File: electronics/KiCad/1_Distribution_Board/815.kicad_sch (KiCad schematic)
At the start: 10 parts, among them J1 Conn_02x08_Odd_Even, J40 Module Right, J42 Signals 0-3, J43 Signals 4-7, J44 Signals 8-11, J45 Conn_01x10, J46 Conn_01x06, J47 Signals 12-15, J48 Module Left

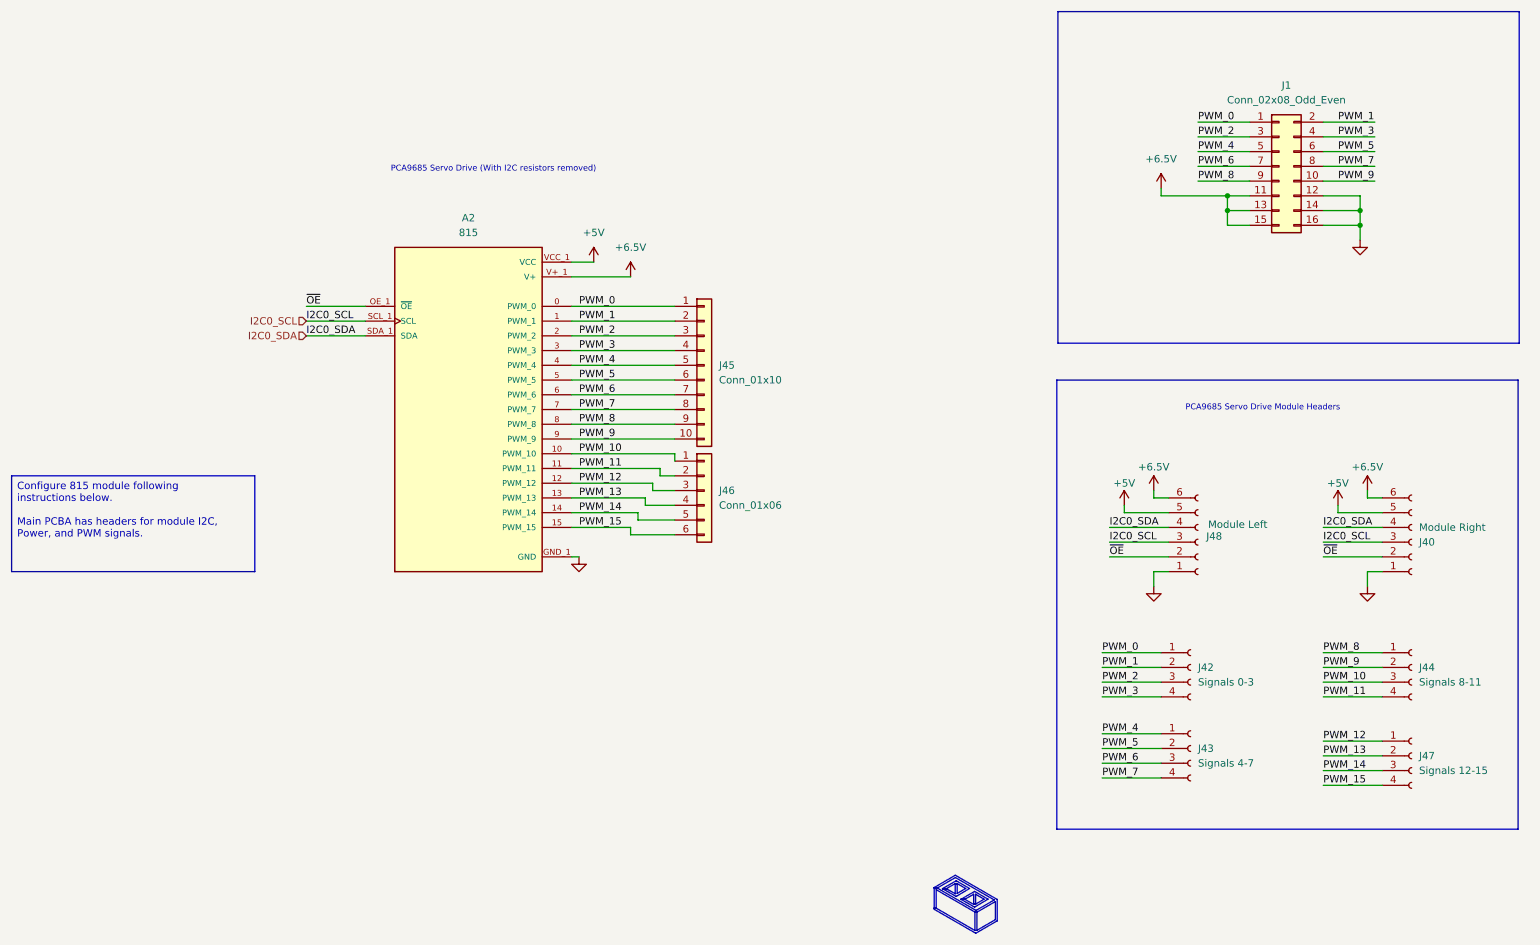
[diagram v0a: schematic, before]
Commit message: PCB updates
Added stepper module headers and working on silk for ease of debug.
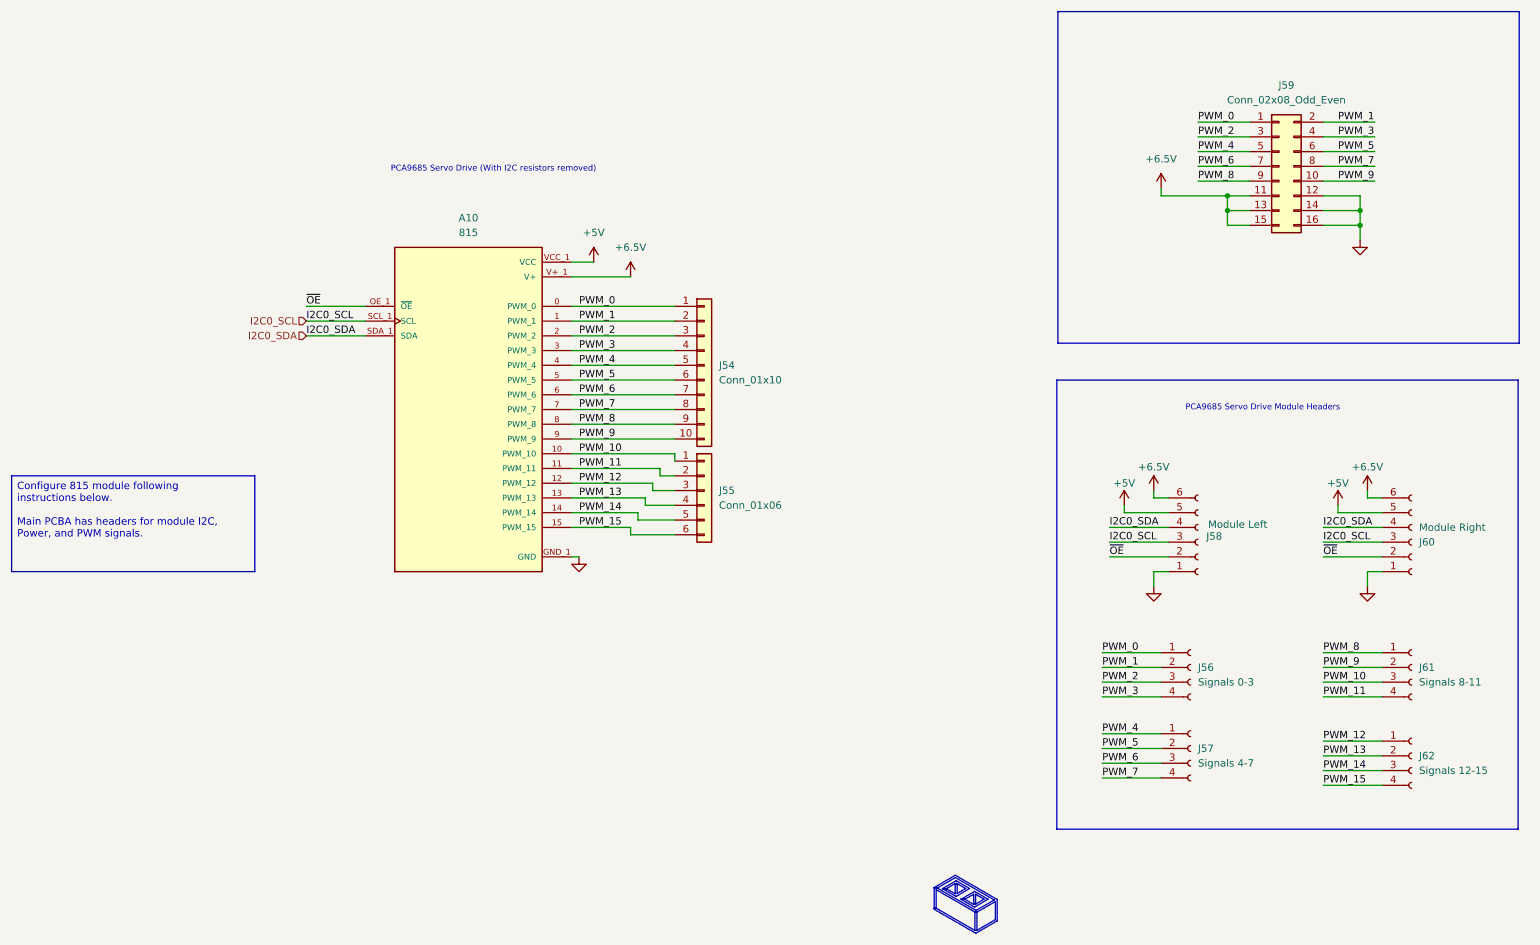
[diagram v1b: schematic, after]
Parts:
- renumbered A2 to A10, J45 to J54, J46 to J55, J42 to J56, J43 to J57, J48 to J58, J1 to J59, J40 to J60, J44 to J61, J47 to J62
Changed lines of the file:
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@@
 		(dnp no)
 		(fields_autoplaced yes)
-		(property "Reference" "J46"
+		(property "Reference" "J55"
 			(at 140.97 101.5999 0)
 			(effects
@@
 			(project "1_Distribution_Board"
 				(path "/d53c8c01-e754-4310-8a73-7d7c95e64cd3/4f60e607-b8a0-4b26-ada7-74dd2d095020"
-					(reference "J46")
+					(reference "J55")
 					(unit 1)
 				)
@@
 		(dnp no)
 		(fields_autoplaced yes)
-		(property "Reference" "#PWR0110"
+		(property "Reference" "#PWR0135"
 			(at 251.46 64.77 0)
 			(effects
@@
 			(project "1_Distribution_Board"
 				(path "/d53c8c01-e754-4310-8a73-7d7c95e64cd3/4f60e607-b8a0-4b26-ada7-74dd2d095020"
-					(reference "#PWR0110")
+					(reference "#PWR0135")
 					(unit 1)
 				)
@@
 		(dnp no)
 		(fields_autoplaced yes)
-		(property "Reference" "#PWR0109"
+		(property "Reference" "#PWR0133"
 			(at 217.17 53.34 0)
 			(effects
@@
 			(project "1_Distribution_Board"
 				(path "/d53c8c01-e754-4310-8a73-7d7c95e64cd3/4f60e607-b8a0-4b26-ada7-74dd2d095020"
-					(reference "#PWR0109")
+					(reference "#PWR0133")
 					(unit 1)
 				)
@@
 		(dnp no)
 		(fields_autoplaced yes)
-		(property "Reference" "J45"
+		(property "Reference" "J54"
 			(at 140.97 80.0099 0)
 			(effects
@@
 			(project "1_Distribution_Board"
 				(path "/d53c8c01-e754-4310-8a73-7d7c95e64cd3/4f60e607-b8a0-4b26-ada7-74dd2d095020"
-					(reference "J45")
+					(reference "J54")
 					(unit 1)
 				)
@@
 		(dnp no)
 		(fields_autoplaced yes)
-		(property "Reference" "J1"
+		(property "Reference" "J59"
 			(at 238.76 31.75 0)
 			(effects
@@
 			(project "1_Distribution_Board"
 				(path "/d53c8c01-e754-4310-8a73-7d7c95e64cd3/4f60e607-b8a0-4b26-ada7-74dd2d095020"
-					(reference "J1")
+					(reference "J59")
 					(unit 1)
 				)
@@
 		(on_board yes)
 		(dnp no)
-		(property "Reference" "#PWR0112"
+		(property "Reference" "#PWR0134"
 			(at 247.65 107.95 0)
 			(effects
@@
 			(project "1_Distribution_Board"
 				(path "/d53c8c01-e754-4310-8a73-7d7c95e64cd3/4f60e607-b8a0-4b26-ada7-74dd2d095020"
-					(reference "#PWR0112")
+					(reference "#PWR0134")
 					(unit 1)
 				)
@@
 		(dnp no)
 		(fields_autoplaced yes)
-		(property "Reference" "J44"
+		(property "Reference" "J61"
 			(at 261.62 132.0799 0)
 			(effects
@@
 			(project "1_Distribution_Board"
 				(path "/d53c8c01-e754-4310-8a73-7d7c95e64cd3/4f60e607-b8a0-4b26-ada7-74dd2d095020"
-					(reference "J44")
+					(reference "J61")
 					(unit 1)
 				)
@@
 		(on_board yes)
 		(dnp no)
-		(property "Reference" "#PWR0113"
+		(property "Reference" "#PWR0136"
 			(at 252.73 105.41 0)
 			(effects
@@
 			(project "1_Distribution_Board"
 				(path "/d53c8c01-e754-4310-8a73-7d7c95e64cd3/4f60e607-b8a0-4b26-ada7-74dd2d095020"
-					(reference "#PWR0113")
+					(reference "#PWR0136")
 					(unit 1)
 				)
@@
 		(dnp no)
 		(fields_autoplaced yes)
-		(property "Reference" "J43"
+		(property "Reference" "J57"
 			(at 223.52 146.0499 0)
 			(effects
@@
 			(project "1_Distribution_Board"
 				(path "/d53c8c01-e754-4310-8a73-7d7c95e64cd3/4f60e607-b8a0-4b26-ada7-74dd2d095020"
-					(reference "J43")
+					(reference "J57")
 					(unit 1)
 				)
@@
 		(dnp no)
 		(fields_autoplaced yes)
-		(property "Reference" "#PWR0111"
+		(property "Reference" "#PWR0137"
 			(at 252.73 124.46 0)
 			(effects
@@
 			(project "1_Distribution_Board"
 				(path "/d53c8c01-e754-4310-8a73-7d7c95e64cd3/4f60e607-b8a0-4b26-ada7-74dd2d095020"
-					(reference "#PWR0111")
+					(reference "#PWR0137")
 					(unit 1)
 				)
@@
 		(dnp no)
 		(fields_autoplaced yes)
-		(property "Reference" "J42"
+		(property "Reference" "J56"
 			(at 223.52 132.0799 0)
 			(effects
@@
 			(project "1_Distribution_Board"
 				(path "/d53c8c01-e754-4310-8a73-7d7c95e64cd3/4f60e607-b8a0-4b26-ada7-74dd2d095020"
-					(reference "J42")
+					(reference "J56")
 					(unit 1)
 				)
@@
 		(dnp no)
 		(fields_autoplaced yes)
-		(property "Reference" "J47"
+		(property "Reference" "J62"
 			(at 261.62 147.3199 0)
 			(effects
@@
 			(project "1_Distribution_Board"
 				(path "/d53c8c01-e754-4310-8a73-7d7c95e64cd3/4f60e607-b8a0-4b26-ada7-74dd2d095020"
-					(reference "J47")
+					(reference "J62")
 					(unit 1)
 				)
@@
 		(dnp no)
 		(fields_autoplaced yes)
-		(property "Reference" "#PWR0116"
+		(property "Reference" "#PWR0132"
 			(at 215.9 124.46 0)
 			(effects
@@
 			(project "1_Distribution_Board"
 				(path "/d53c8c01-e754-4310-8a73-7d7c95e64cd3/4f60e607-b8a0-4b26-ada7-74dd2d095020"
-					(reference "#PWR0116")
+					(reference "#PWR0132")
 					(unit 1)
 				)
@@
 		(dnp no)
 		(fields_autoplaced yes)
-		(property "Reference" "#PWR011"
+		(property "Reference" "#PWR0128"
 			(at 119.38 66.04 0)
 			(effects
@@
 			(project "1_Distribution_Board"
 				(path "/d53c8c01-e754-4310-8a73-7d7c95e64cd3/4f60e607-b8a0-4b26-ada7-74dd2d095020"
-					(reference "#PWR011")
+					(reference "#PWR0128")
 					(unit 1)
 				)
@@
 		(dnp no)
 		(fields_autoplaced yes)
-		(property "Reference" "#PWR012"
+		(property "Reference" "#PWR0129"
 			(at 125.73 68.58 0)
 			(effects
@@
 			(project "1_Distribution_Board"
 				(path "/d53c8c01-e754-4310-8a73-7d7c95e64cd3/4f60e607-b8a0-4b26-ada7-74dd2d095020"
-					(reference "#PWR012")
+					(reference "#PWR0129")
 					(unit 1)
 				)
@@
 		(on_board yes)
 		(dnp no)
-		(property "Reference" "#PWR0115"
+		(property "Reference" "#PWR0131"
 			(at 215.9 105.41 0)
 			(effects
@@
 			(project "1_Distribution_Board"
 				(path "/d53c8c01-e754-4310-8a73-7d7c95e64cd3/4f60e607-b8a0-4b26-ada7-74dd2d095020"
-					(reference "#PWR0115")
+					(reference "#PWR0131")
 					(unit 1)
 				)
@@
 		(dnp no)
 		(fields_autoplaced yes)
-		(property "Reference" "A2"
+		(property "Reference" "A10"
 			(at 97.79 54.61 0)
 			(effects
@@
 			(project "1_Distribution_Board"
 				(path "/d53c8c01-e754-4310-8a73-7d7c95e64cd3/4f60e607-b8a0-4b26-ada7-74dd2d095020"
-					(reference "A2")
+					(reference "A10")
 					(unit 1)
 				)
@@
 		(dnp no)
 		(fields_autoplaced yes)
-		(property "Reference" "J40"
+		(property "Reference" "J60"
 			(at 261.62 110.4901 0)
 			(effects
@@
 			(project "1_Distribution_Board"
 				(path "/d53c8c01-e754-4310-8a73-7d7c95e64cd3/4f60e607-b8a0-4b26-ada7-74dd2d095020"
-					(reference "J40")
+					(reference "J60")
 					(unit 1)
 				)
@@
 		(on_board yes)
 		(dnp no)
-		(property "Reference" "#PWR0114"
+		(property "Reference" "#PWR0130"
 			(at 210.82 107.95 0)
 			(effects
@@
 			(project "1_Distribution_Board"
 				(path "/d53c8c01-e754-4310-8a73-7d7c95e64cd3/4f60e607-b8a0-4b26-ada7-74dd2d095020"
-					(reference "#PWR0114")
+					(reference "#PWR0130")
 					(unit 1)
 				)
@@
 		(on_board yes)
 		(dnp no)
-		(property "Reference" "J48"
+		(property "Reference" "J58"
 			(at 226.314 109.474 0)
 			(effects
@@
 			(project "1_Distribution_Board"
 				(path "/d53c8c01-e754-4310-8a73-7d7c95e64cd3/4f60e607-b8a0-4b26-ada7-74dd2d095020"
-					(reference "J48")
+					(reference "J58")
 					(unit 1)
 				)
@@
 		(dnp no)
 		(fields_autoplaced yes)
-		(property "Reference" "#PWR010"
+		(property "Reference" "#PWR0127"
 			(at 116.84 119.38 0)
 			(effects
@@
 			(project "1_Distribution_Board"
 				(path "/d53c8c01-e754-4310-8a73-7d7c95e64cd3/4f60e607-b8a0-4b26-ada7-74dd2d095020"
-					(reference "#PWR010")
-					(unit 1)
-				)
+					(reference "#PWR0127")
+					(unit 1)
+				)

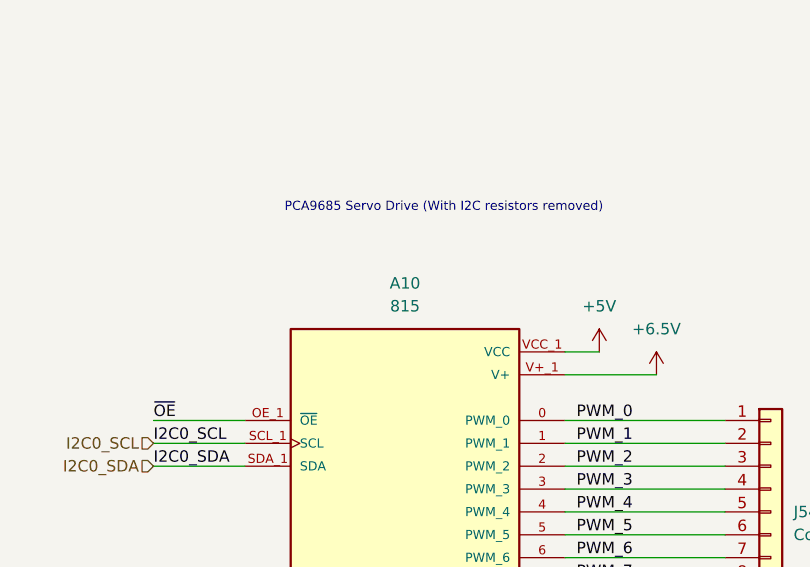
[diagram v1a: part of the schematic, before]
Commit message: Updated PCB/SCH
Updated stepper schematics and motor schematics for clarity. Updated motor module to use headers. Updated stepper driver top be the BIGTREETECH V1.3. Cleaned up layout locations a bit.
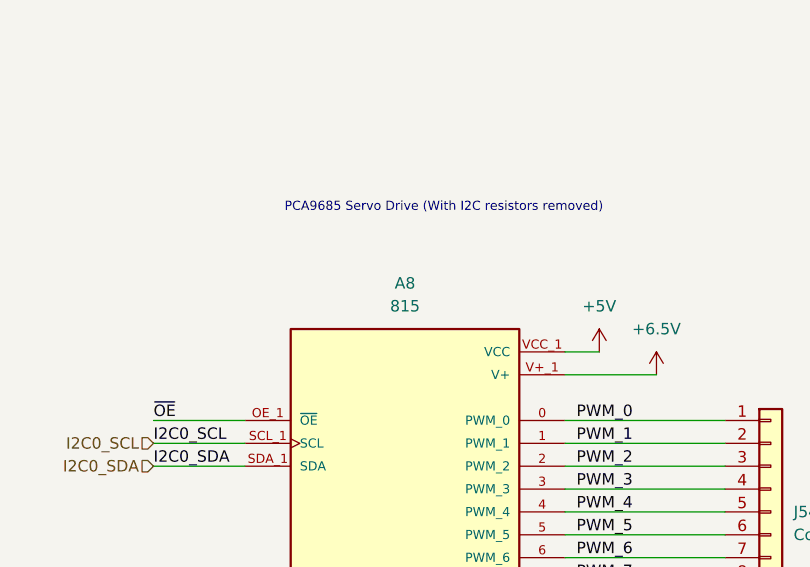
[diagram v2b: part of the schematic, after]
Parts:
- renumbered A10 to A8
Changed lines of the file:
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@@
 		(dnp no)
 		(fields_autoplaced yes)
-		(property "Reference" "A10"
+		(property "Reference" "A8"
 			(at 97.79 54.61 0)
 			(effects
@@
 			(project "1_Distribution_Board"
 				(path "/d53c8c01-e754-4310-8a73-7d7c95e64cd3/4f60e607-b8a0-4b26-ada7-74dd2d095020"
-					(reference "A10")
+					(reference "A8")
 					(unit 1)
 				)

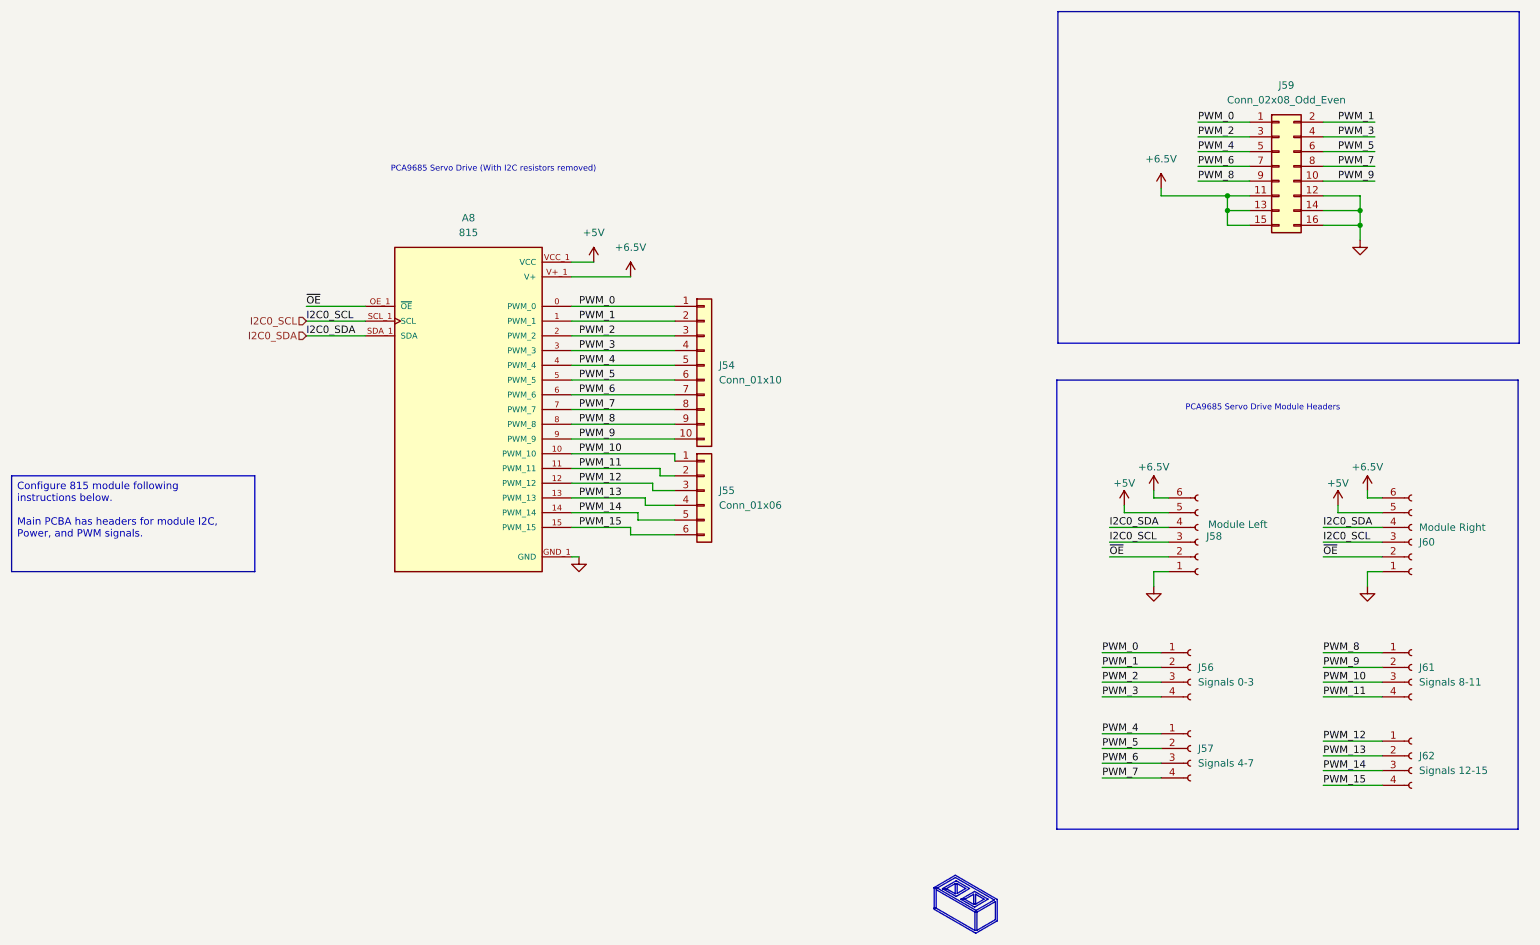
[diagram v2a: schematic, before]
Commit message: Additional Routing and placement
Updated power page on schematic to remove redundant connections. Removed test points on steppers since the steppers drivers chosen have test points on them. Updated placement and cleaned up silk. Started placing final power connections.
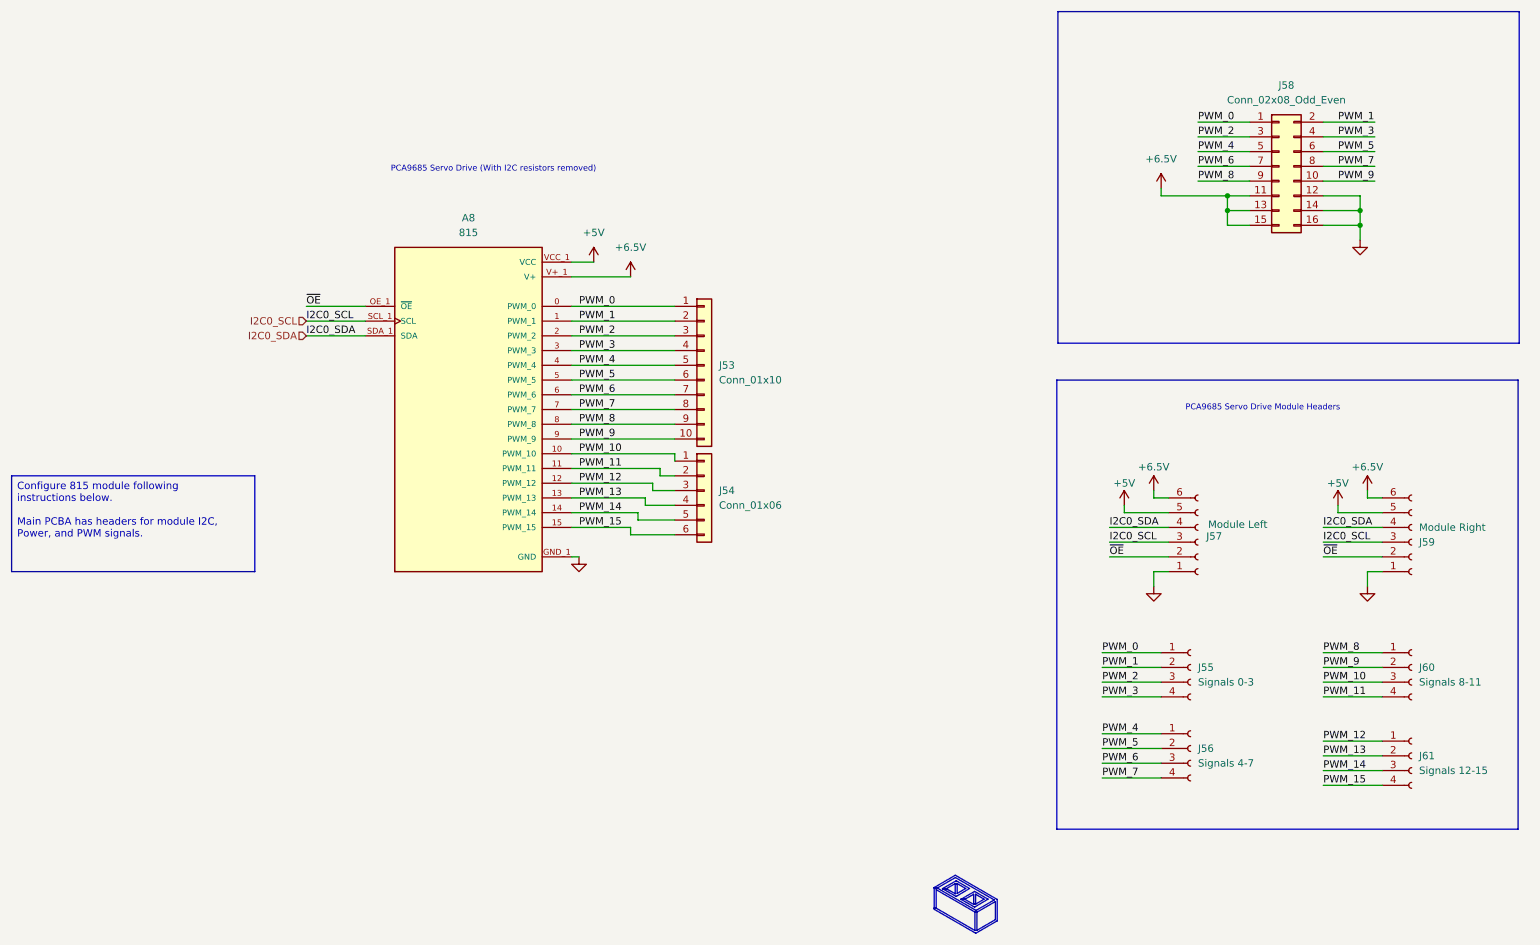
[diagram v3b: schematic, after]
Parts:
- renumbered J54 to J53, J55 to J54, J56 to J55, J57 to J56, J58 to J57, J59 to J58, J60 to J59, J61 to J60, J62 to J61
